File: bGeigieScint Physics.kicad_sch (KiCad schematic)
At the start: 19 parts, among them IC1 MICROFJ-60035-TSV-TR, P1 Header-Male-2.54_2x2, P2 Header-Male-2.54_2x2, U1 TMP116xxDRV, U2 AT24CS01-STUM

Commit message: Refactor code structure for improved readability and maintainability
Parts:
- removed H3: MountingHole, MountingHole:MountingHole_3.2mm_M3, symbol Mechanical:MountingHole
- P1, P2: footprint Connector_PinHeader_2.54mm:PinHeader_2x02_P2.54mm_Vertical -> Connector_PinHeader_2.54mm:PinHeader_2x02_P2.54mm_Vertical_SMD
- R1, R3, R4, R5: footprint (none) -> Resistor_SMD:R_0805_2012Metric
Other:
- company: Safecast -> Sensor board for bGeigieScint
- moved on the sheet: H4
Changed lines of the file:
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@@
 	(title_block
 		(title "bGeigieScint Physics")
-		(date "2025-12-31")
+		(date "2026-01-05")
 		(rev "0.9")
-		(company "Safecast")
+		(company "Sensor board for bGeigieScint")
+		(comment 1 "Safecast ")
 	)
 	(junction
@@
 	(wire
 		(pts
-			(xy 167.005 113.665) (xy 167.005 122.555)
+			(xy 167.005 113.665) (xy 167.005 121.285)
 		)
 		(stroke
@@
 			)
 		)
-		(property "Footprint" "Connector_PinHeader_2.54mm:PinHeader_2x02_P2.54mm_Vertical"
+		(property "Footprint" "Connector_PinHeader_2.54mm:PinHeader_2x02_P2.54mm_Vertical_SMD"
 			(at 157.48 71.755 0)
 			(effects
@@
 	(symbol
 		(lib_id "power:GND")
-		(at 167.005 122.555 0)
+		(at 167.005 121.285 0)
 		(unit 1)
 		(exclude_from_sim no)
@@
 		(fields_autoplaced yes)
 		(property "Reference" "#PWR09"
-			(at 167.005 128.905 0)
+			(at 167.005 127.635 0)
 			(effects
 				(font
@@
 		)
 		(property "Value" "GND"
-			(at 167.005 127.635 0)
+			(at 167.005 126.365 0)
 			(effects
 				(font
@@
 		)
 		(property "Footprint" ""
-			(at 167.005 122.555 0)
+			(at 167.005 121.285 0)
 			(effects
 				(font
@@
 		)
 		(property "Datasheet" ""
-			(at 167.005 122.555 0)
+			(at 167.005 121.285 0)
 			(effects
 				(font
@@
 		)
 		(property "Description" "Power symbol creates a global label with name \"GND\" , ground"
-			(at 167.005 122.555 0)
+			(at 167.005 121.285 0)
 			(effects
 				(font
@@
 	(symbol
 		(lib_id "Mechanical:MountingHole")
-		(at 264.795 156.845 0)
+		(at 257.175 157.48 0)
 		(unit 1)
 		(exclude_from_sim no)
@@
 		(fields_autoplaced yes)
 		(property "Reference" "H4"
-			(at 267.97 155.5749 0)
+			(at 260.35 156.2099 0)
 			(effects
 				(font
@@
 		)
 		(property "Value" "MountingHole"
-			(at 267.97 158.1149 0)
+			(at 260.35 158.7499 0)
 			(effects
 				(font
@@
 		)
 		(property "Footprint" "MountingHole:MountingHole_3.2mm_M3"
-			(at 264.795 156.845 0)
+			(at 257.175 157.48 0)
 			(effects
 				(font
@@
 		)
 		(property "Datasheet" "~"
-			(at 264.795 156.845 0)
+			(at 257.175 157.48 0)
 			(effects
 				(font
@@
 		)
 		(property "Description" "Mounting Hole without connection"
-			(at 264.795 156.845 0)
+			(at 257.175 157.48 0)
 			(effects
 				(font
@@
 			)
 		)
-		(property "Footprint" "Connector_PinHeader_2.54mm:PinHeader_2x02_P2.54mm_Vertical"
+		(property "Footprint" "Connector_PinHeader_2.54mm:PinHeader_2x02_P2.54mm_Vertical_SMD"
 			(at 128.27 71.755 0)
 			(effects
@@
 			)
 		)
-		(property "Footprint" ""
+		(property "Footprint" "Resistor_SMD:R_0805_2012Metric"
 			(at 90.805 101.6 0)
 			(effects
@@
 					(size 1.27 1.27)
 				)
+				(hide yes)
 			)
 		)
@@
 			)
 		)
-		(property "Footprint" ""
+		(property "Footprint" "Resistor_SMD:R_0805_2012Metric"
 			(at 139.7 90.805 0)
 			(effects
@@
 					(size 1.27 1.27)
 				)
+				(hide yes)
 			)
 		)
@@
 	)
 	(symbol
-		(lib_id "Mechanical:MountingHole")
-		(at 256.54 156.845 0)
-		(unit 1)
-		(exclude_from_sim no)
-		(in_bom no)
-		(on_board yes)
-		(dnp no)
-		(fields_autoplaced yes)
-		(property "Reference" "H3"
-			(at 259.715 155.5749 0)
-			(effects
-				(font
-					(size 1.27 1.27)
-				)
-				(justify left)
-			)
-		)
-		(property "Value" "MountingHole"
-			(at 259.715 158.1149 0)
-			(effects
-				(font
-					(size 1.27 1.27)
-				)
-				(justify left)
-			)
-		)
-		(property "Footprint" "MountingHole:MountingHole_3.2mm_M3"
-			(at 256.54 156.845 0)
-			(effects
-				(font
-					(size 1.27 1.27)
-				)
-				(hide yes)
-			)
-		)
-		(property "Datasheet" "~"
-			(at 256.54 156.845 0)
-			(effects
-				(font
-					(size 1.27 1.27)
-				)
-				(hide yes)
-			)
-		)
-		(property "Description" "Mounting Hole without connection"
-			(at 256.54 156.845 0)
-			(effects
-				(font
-					(size 1.27 1.27)
-				)
-				(hide yes)
-			)
-		)
-		(instances
-			(project "bGeigieScint Physics"
-				(path "/5482910c-3562-491e-9203-123456789abc"
-					(reference "H3")
-					(unit 1)
-				)
-			)
-		)
-	)
-	(symbol
 		(lib_id "power:GND")
 		(at 35.56 92.71 0)
@@
 			)
 		)
-		(property "Footprint" ""
+		(property "Footprint" "Resistor_SMD:R_0805_2012Metric"
 			(at 135.255 90.805 0)
 			(effects
@@
 					(size 1.27 1.27)
 				)
+				(hide yes)
 			)
 		)
@@
 			)
 		)
-		(property "Footprint" ""
+		(property "Footprint" "Resistor_SMD:R_0805_2012Metric"
 			(at 63.5 101.6 0)
 			(effects
@@
 					(size 1.27 1.27)
 				)
-			)
-		)
+				(hide yes)
+			)
+		)

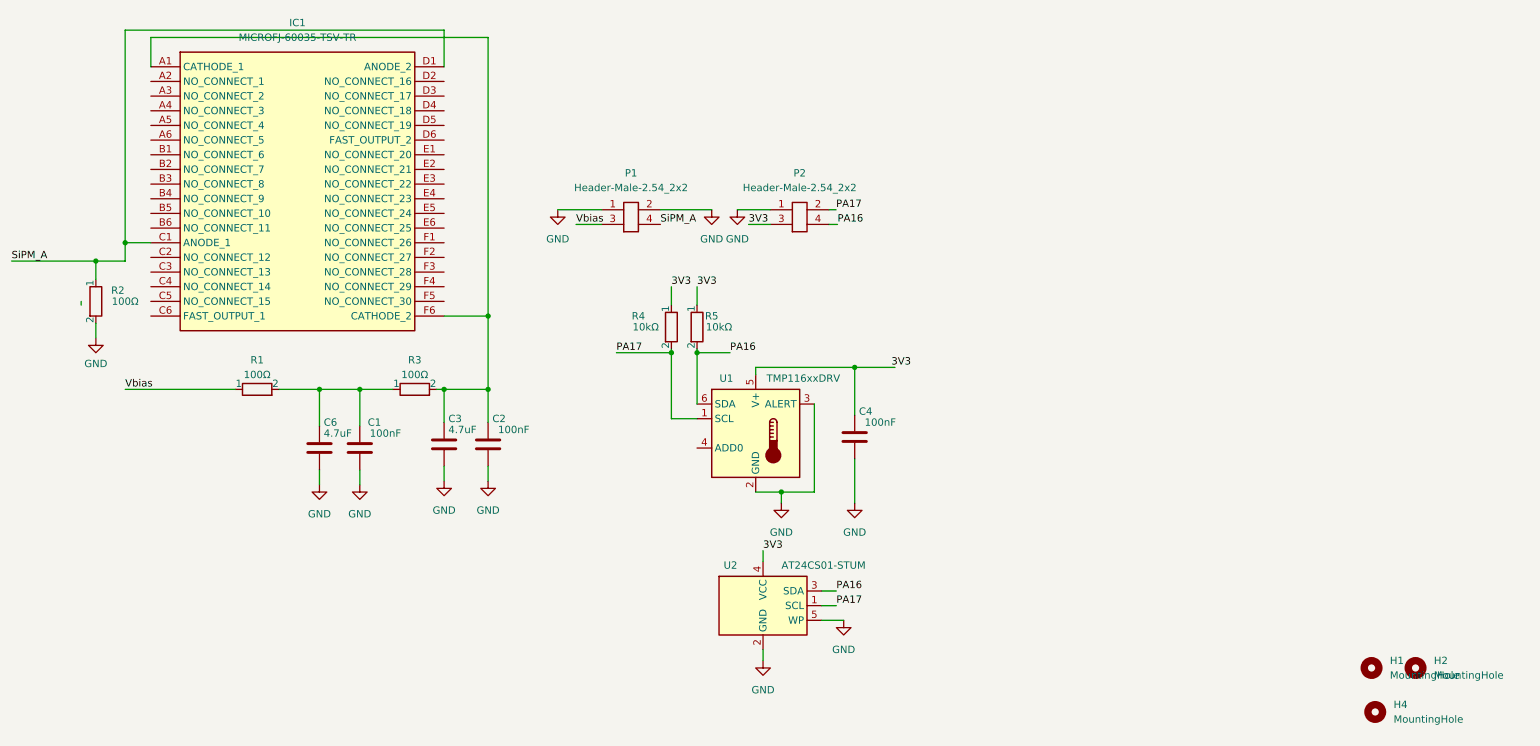
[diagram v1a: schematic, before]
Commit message: Added 3d model files, how to build files, etc
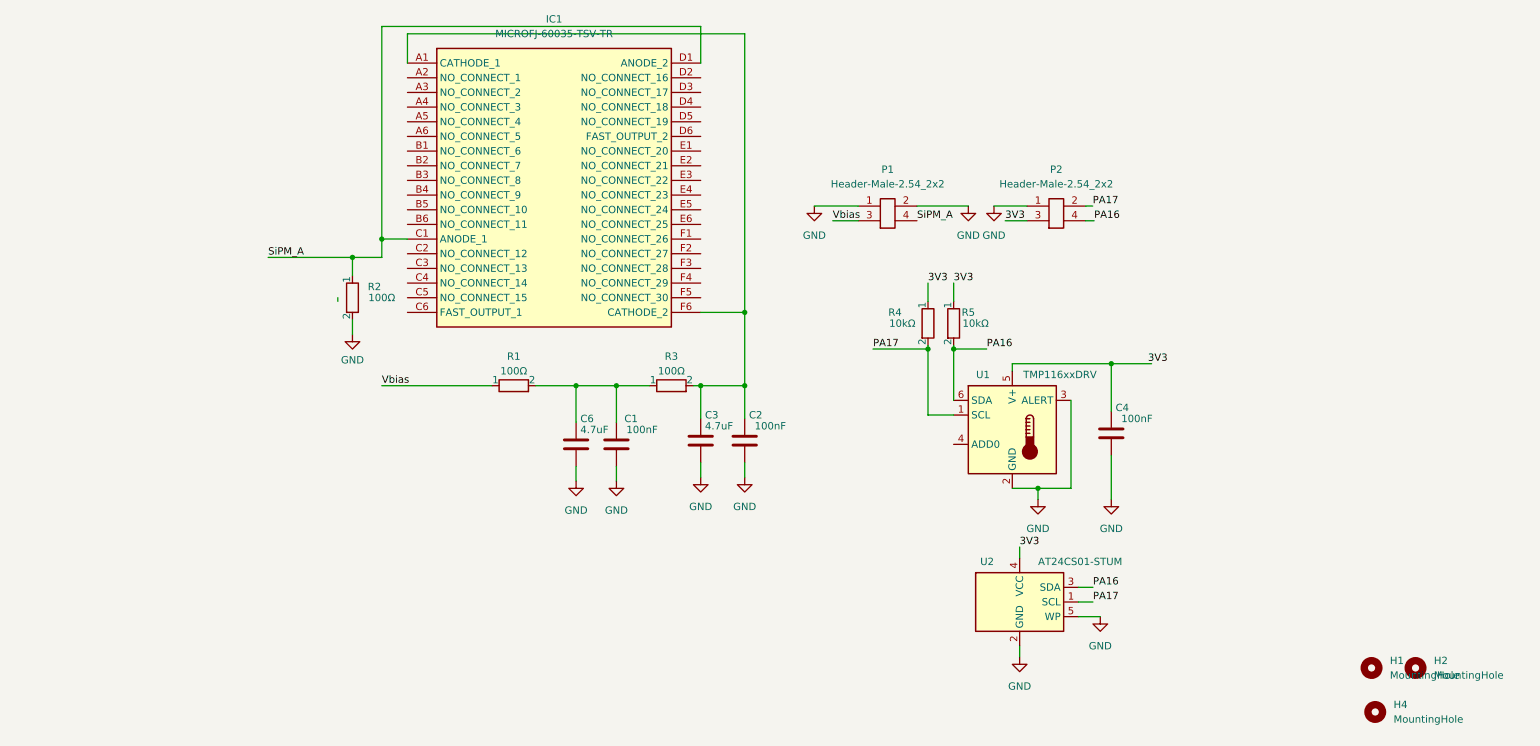
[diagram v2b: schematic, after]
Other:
- moved on the sheet: C1, C2, C3, C4, C6, IC1, P1, P2, R1, R2, R3, R4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

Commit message: Refactor code structure for improved readability and maintainability
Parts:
- added H3: MountingHole, MountingHole:MountingHole_3.2mm_M3, symbol Mechanical:MountingHole
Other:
- moved on the sheet: H4
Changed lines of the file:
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@@
 	(symbol
 		(lib_id "Mechanical:MountingHole")
-		(at 257.175 157.48 0)
+		(at 264.16 158.75 0)
 		(unit 1)
 		(exclude_from_sim no)
@@
 		(fields_autoplaced yes)
 		(property "Reference" "H4"
-			(at 260.35 156.2099 0)
+			(at 267.335 157.4799 0)
 			(effects
 				(font
@@
 		)
 		(property "Value" "MountingHole"
-			(at 260.35 158.7499 0)
+			(at 267.335 160.0199 0)
 			(effects
 				(font
@@
 		)
 		(property "Footprint" "MountingHole:MountingHole_3.2mm_M3"
-			(at 257.175 157.48 0)
+			(at 264.16 158.75 0)
 			(effects
 				(font
@@
 		)
 		(property "Datasheet" "~"
-			(at 257.175 157.48 0)
+			(at 264.16 158.75 0)
 			(effects
 				(font
@@
 		)
 		(property "Description" "Mounting Hole without connection"
-			(at 257.175 157.48 0)
+			(at 264.16 158.75 0)
 			(effects
 				(font
@@
 					(unit 1)
 				)
+			)
+		)
+	)
+	(symbol
+		(lib_id "Mechanical:MountingHole")
+		(at 256.54 158.75 0)
+		(unit 1)
+		(exclude_from_sim no)
+		(in_bom no)
+		(on_board yes)
+		(dnp no)
+		(fields_autoplaced yes)
+		(property "Reference" "H3"
+			(at 259.715 157.4799 0)
+			(effects
+				(font
+					(size 1.27 1.27)
+				)
+				(justify left)
+			)
+		)
+		(property "Value" "MountingHole"
+			(at 259.715 160.0199 0)
+			(effects
+				(font
+					(size 1.27 1.27)
+				)
+				(justify left)
+			)
+		)
+		(property "Footprint" "MountingHole:MountingHole_3.2mm_M3"
+			(at 256.54 158.75 0)
+			(effects
+				(font
+					(size 1.27 1.27)
+				)
+				(hide yes)
+			)
+		)
+		(property "Datasheet" "~"
+			(at 256.54 158.75 0)
+			(effects
+				(font
+					(size 1.27 1.27)
+				)
+				(hide yes)
+			)
+		)
+		(property "Description" "Mounting Hole without connection"
+			(at 256.54 158.75 0)
+			(effects
+				(font
+					(size 1.27 1.27)
+				)
+				(hide yes)
+			)
+		)
+		(instances
+			(project "bGeigieScint Physics"
+				(path "/5482910c-3562-491e-9203-123456789abc"
+					(reference "H3")
+					(unit 1)
+				)

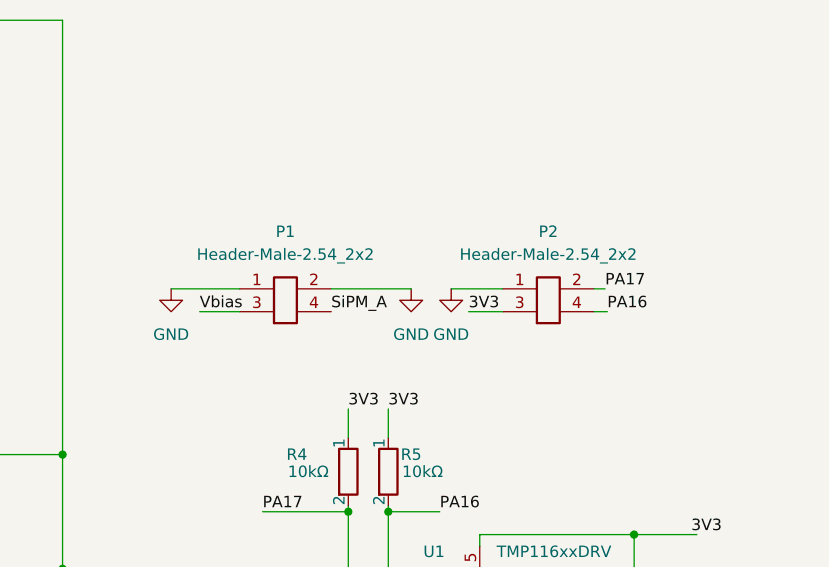
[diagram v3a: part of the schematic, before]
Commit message: - Added initial entries for various components including capacitors, resistors, and headers.T right angle counts
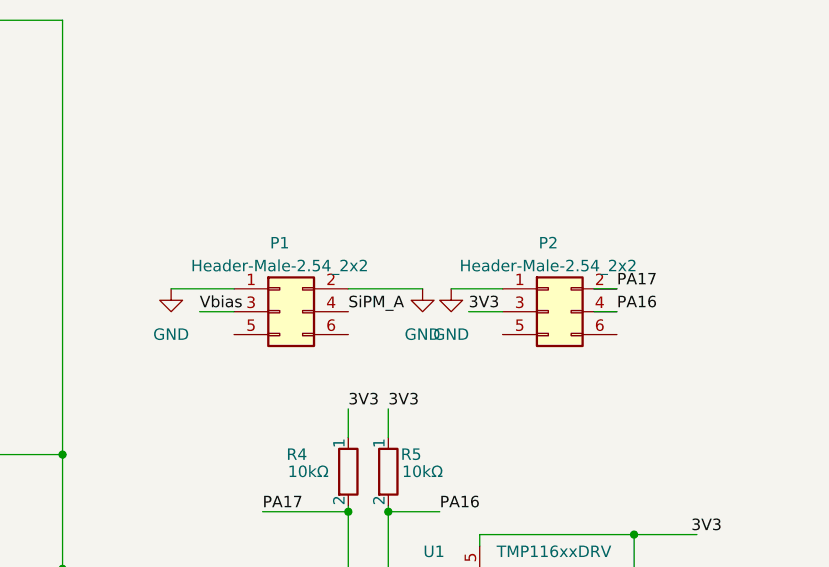
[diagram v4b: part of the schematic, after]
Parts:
- P1, P2: footprint Connector_PinHeader_2.54mm:PinHeader_2x02_P2.54mm_Vertical_SMD -> Connector_PinHeader_2.54mm:PinHeader_2x03_P2.54mm_Vertical_SMD; symbol Header_2x2 -> Connector_Generic:Conn_02x03_Odd_Even
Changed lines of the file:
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@@
-	(wire
-		(pts
-			(xy 177.8 69.85) (xy 186.69 69.85)
-		)
-		(stroke
-			(width 0)
-			(type default)
-		)
-	)
 	(wire
 		(pts
@@
 	(wire
 		(pts
-			(xy 208.4791 72.39) (xy 207.01 72.39)
+			(xy 167.005 69.85) (xy 160.02 69.85)
+		)
+		(stroke
+			(width 0)
+			(type default)
+		)
+	)
+	(wire
+		(pts
+			(xy 209.55 72.39) (xy 207.01 72.39)
 		)
 		(stroke
@@
 	(wire
 		(pts
+			(xy 179.705 69.85) (xy 187.96 69.85)
+		)
+		(stroke
+			(width 0)
+			(type default)
+		)
+	)
+	(wire
+		(pts
 			(xy 111.76 100.965) (xy 118.745 100.965)
 		)
@@
 	(wire
 		(pts
+			(xy 163.195 72.39) (xy 167.005 72.39)
+		)
+		(stroke
+			(width 0)
+			(type default)
+		)
+	)
+	(wire
+		(pts
 			(xy 140.335 100.965) (xy 147.955 100.965)
 		)
@@
 	(wire
 		(pts
-			(xy 163.195 72.39) (xy 167.64 72.39)
-		)
-		(stroke
-			(width 0)
-			(type default)
-		)
-	)
-	(wire
-		(pts
 			(xy 179.705 94.615) (xy 179.705 106.045)
 		)
@@
 	(wire
 		(pts
-			(xy 160.02 69.85) (xy 167.64 69.85)
-		)
-		(stroke
-			(width 0)
-			(type default)
-		)
-	)
-	(wire
-		(pts
 			(xy 193.0778 72.39) (xy 196.85 72.39)
 		)
@@
 	(wire
 		(pts
-			(xy 208.2355 69.85) (xy 207.01 69.85)
+			(xy 209.55 69.85) (xy 207.01 69.85)
 		)
 		(stroke
@@
 		)
 	)
-	(label "SiPM_A"
-		(at 177.8 72.39 0)
-		(effects
-			(font
-				(size 1.27 1.27)
-			)
-			(justify left bottom)
-		)
-	)
 	(label "3V3"
 		(at 193.0778 72.39 0)
@@
 	)
 	(label "PA16"
-		(at 208.4791 72.39 0)
+		(at 209.55 72.39 0)
 		(effects
 			(font
@@
 	)
 	(label "PA17"
-		(at 208.2355 69.85 0)
+		(at 209.55 69.85 0)
 		(effects
 			(font
@@
 	(label "3V3"
 		(at 195.58 128.905 0)
+		(effects
+			(font
+				(size 1.27 1.27)
+			)
+			(justify left bottom)
+		)
+	)
+	(label "SiPM_A"
+		(at 179.705 72.39 0)
 		(effects
 			(font
@@
 	)
 	(symbol
-		(lib_id "Header_2x2")
-		(at 201.93 71.12 0)
+		(lib_id "Connector_Generic:Conn_02x03_Odd_Even")
+		(at 201.93 72.39 0)
 		(unit 1)
 		(exclude_from_sim no)
@@
 		(dnp no)
 		(property "Reference" "P2"
-			(at 201.93 63.5 0)
+			(at 201.93 64.77 0)
 			(effects
 				(font
@@
 		)
 		(property "Value" "Header-Male-2.54_2x2"
-			(at 201.93 66.04 0)
-			(effects
-				(font
-					(size 1.27 1.27)
-				)
-			)
-		)
-		(property "Footprint" "Connector_PinHeader_2.54mm:PinHeader_2x02_P2.54mm_Vertical_SMD"
-			(at 201.93 71.12 0)
-			(effects
-				(font
-					(size 1.27 1.27)
-				)
-				(hide yes)
-			)
-		)
-		(property "Datasheet" ""
-			(at 201.93 71.12 0)
-			(effects
-				(font
-					(size 1.27 1.27)
-				)
-			)
-		)
-		(property "Description" ""
-			(at 201.93 71.12 0)
-			(effects
-				(font
-					(size 1.27 1.27)
-				)
+			(at 201.93 67.31 0)
+			(effects
+				(font
+					(size 1.27 1.27)
+				)
+			)
+		)
+		(property "Footprint" "Connector_PinHeader_2.54mm:PinHeader_2x03_P2.54mm_Vertical_SMD"
+			(at 201.93 72.39 0)
+			(effects
+				(font
+					(size 1.27 1.27)
+				)
+				(hide yes)
+			)
+		)
+		(property "Datasheet" "~"
+			(at 201.93 72.39 0)
+			(effects
+				(font
+					(size 1.27 1.27)
+				)
+				(hide yes)
+			)
+		)
+		(property "Description" "Generic connector, double row, 02x03, odd/even pin numbering scheme (row 1 odd numbers, row 2 even numbers), script generated (kicad-library-utils/schlib/autogen/connector/)"
+			(at 201.93 72.39 0)
+			(effects
+				(font
+					(size 1.27 1.27)
+				)
+				(hide yes)
 			)
 		)
@@
 		)
 		(pin "4"
+		)
+		(pin "5"
+		)
+		(pin "6"
 		)
 		(instances
@@
 	(symbol
 		(lib_id "power:GND")
-		(at 186.69 69.85 0)
+		(at 187.96 69.85 0)
 		(unit 1)
 		(exclude_from_sim no)
@@
 		(fields_autoplaced yes)
 		(property "Reference" "#PWR07"
-			(at 186.69 76.2 0)
+			(at 187.96 76.2 0)
 			(effects
 				(font
@@
 		)
 		(property "Value" "GND"
-			(at 186.69 74.93 0)
+			(at 187.96 74.93 0)
 			(effects
 				(font
@@
 		)
 		(property "Footprint" ""
-			(at 186.69 69.85 0)
+			(at 187.96 69.85 0)
 			(effects
 				(font
@@
 		)
 		(property "Datasheet" ""
-			(at 186.69 69.85 0)
+			(at 187.96 69.85 0)
 			(effects
 				(font
@@
 		)
 		(property "Description" "Power symbol creates a global label with name \"GND\" , ground"
-			(at 186.69 69.85 0)
+			(at 187.96 69.85 0)
 			(effects
 				(font
@@
 	)
 	(symbol
-		(lib_id "Header_2x2")
-		(at 172.72 71.12 0)
+		(lib_id "Connector_Generic:Conn_02x03_Odd_Even")
+		(at 172.085 72.39 0)
 		(unit 1)
 		(exclude_from_sim no)
@@
 		(dnp no)
 		(property "Reference" "P1"
-			(at 172.72 63.5 0)
+			(at 172.085 64.77 0)
 			(effects
 				(font
@@
 		)
 		(property "Value" "Header-Male-2.54_2x2"
-			(at 172.72 66.04 0)
-			(effects
-				(font
-					(size 1.27 1.27)
-				)
-			)
-		)
-		(property "Footprint" "Connector_PinHeader_2.54mm:PinHeader_2x02_P2.54mm_Vertical_SMD"
-			(at 172.72 71.12 0)
-			(effects
-				(font
-					(size 1.27 1.27)
-				)
-				(hide yes)
-			)
-		)
-		(property "Datasheet" ""
-			(at 172.72 71.12 0)
-			(effects
-				(font
-					(size 1.27 1.27)
-				)
-			)
-		)
-		(property "Description" ""
-			(at 172.72 71.12 0)
-			(effects
-				(font
-					(size 1.27 1.27)
-				)
+			(at 172.085 67.31 0)
+			(effects
+				(font
+					(size 1.27 1.27)
+				)
+			)
+		)
+		(property "Footprint" "Connector_PinHeader_2.54mm:PinHeader_2x03_P2.54mm_Vertical_SMD"
+			(at 172.085 72.39 0)
+			(effects
+				(font
+					(size 1.27 1.27)
+				)
+				(hide yes)
+			)
+		)
+		(property "Datasheet" "~"
+			(at 172.085 72.39 0)
+			(effects
+				(font
+					(size 1.27 1.27)
+				)
+				(hide yes)
+			)
+		)
+		(property "Description" "Generic connector, double row, 02x03, odd/even pin numbering scheme (row 1 odd numbers, row 2 even numbers), script generated (kicad-library-utils/schlib/autogen/connector/)"
+			(at 172.085 72.39 0)
+			(effects
+				(font
+					(size 1.27 1.27)
+				)
+				(hide yes)
 			)
 		)
@@
 		(pin "4"
 		)
+		(pin "6"
+		)
+		(pin "5"
+		)
 		(instances
